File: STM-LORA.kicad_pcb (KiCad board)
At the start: 2 copper layers, 56.5 x 50.8 mm, 22 parts, among them J1 Batt, J11 CONN_02X09, J13 CONN_01X02, J2 Solar, J3 CONN_01X17, J4 CONN_01X03, J6 CONN_01X01, J9 CONN_01X05, U1 stm32f103c8t6-module-china, U2 RFM95HW

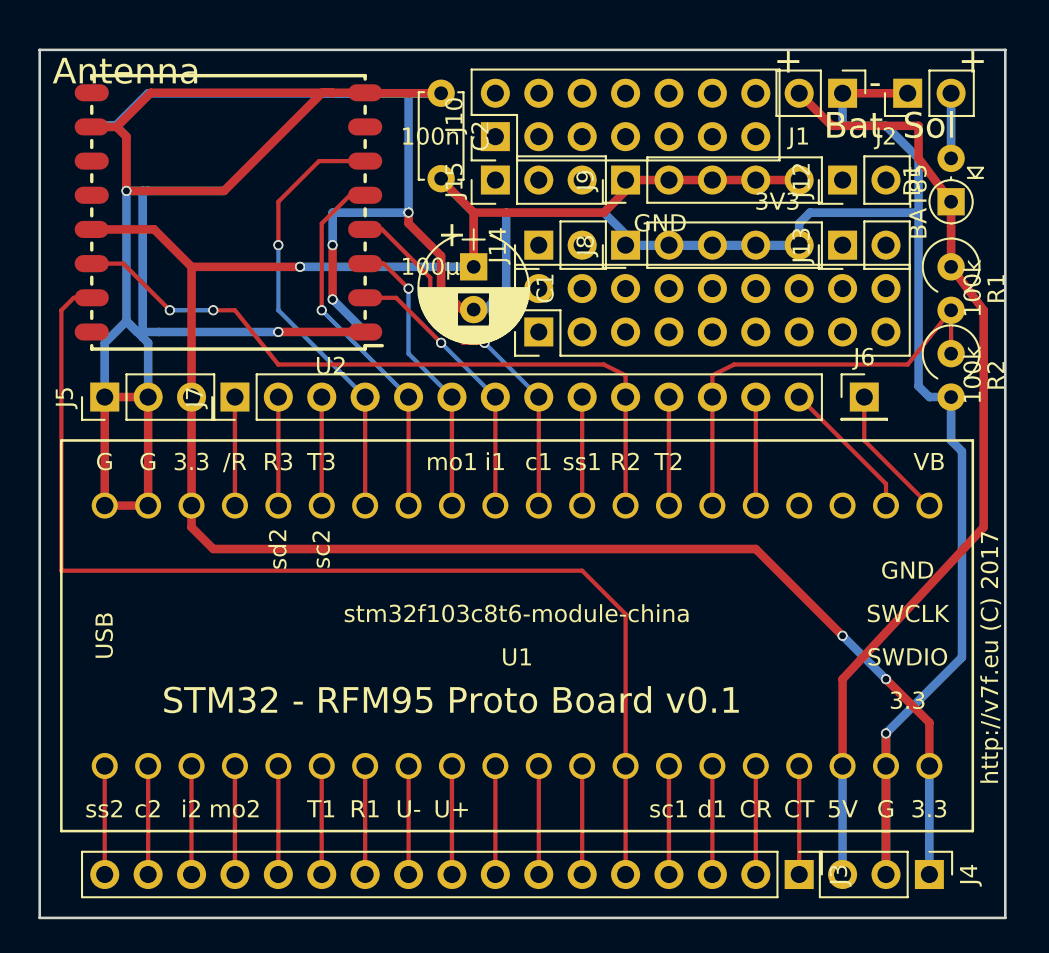
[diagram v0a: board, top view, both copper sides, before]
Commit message: increase power track/via size
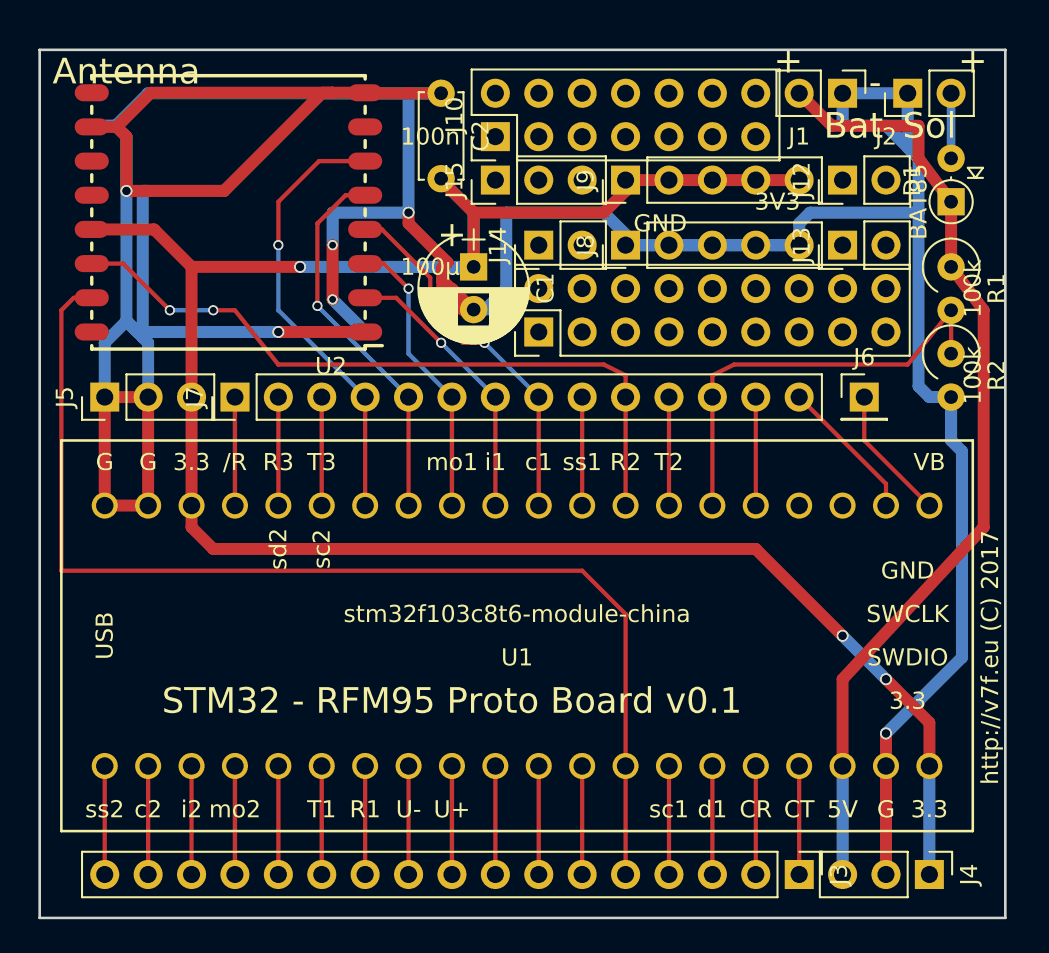
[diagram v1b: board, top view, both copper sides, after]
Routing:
- net GND: track 280.9 -> 290.1 mm
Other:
- net class Power: trace_width 0.5 -> 0.7; via_dia 0.6 -> 0.7; via_drill 0.4 -> 0.5

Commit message: gnd backplane
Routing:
- net GND: track 290.1 -> 21.8 mm, vias 6 -> 4
- added copper zone on B.Cu, net GND

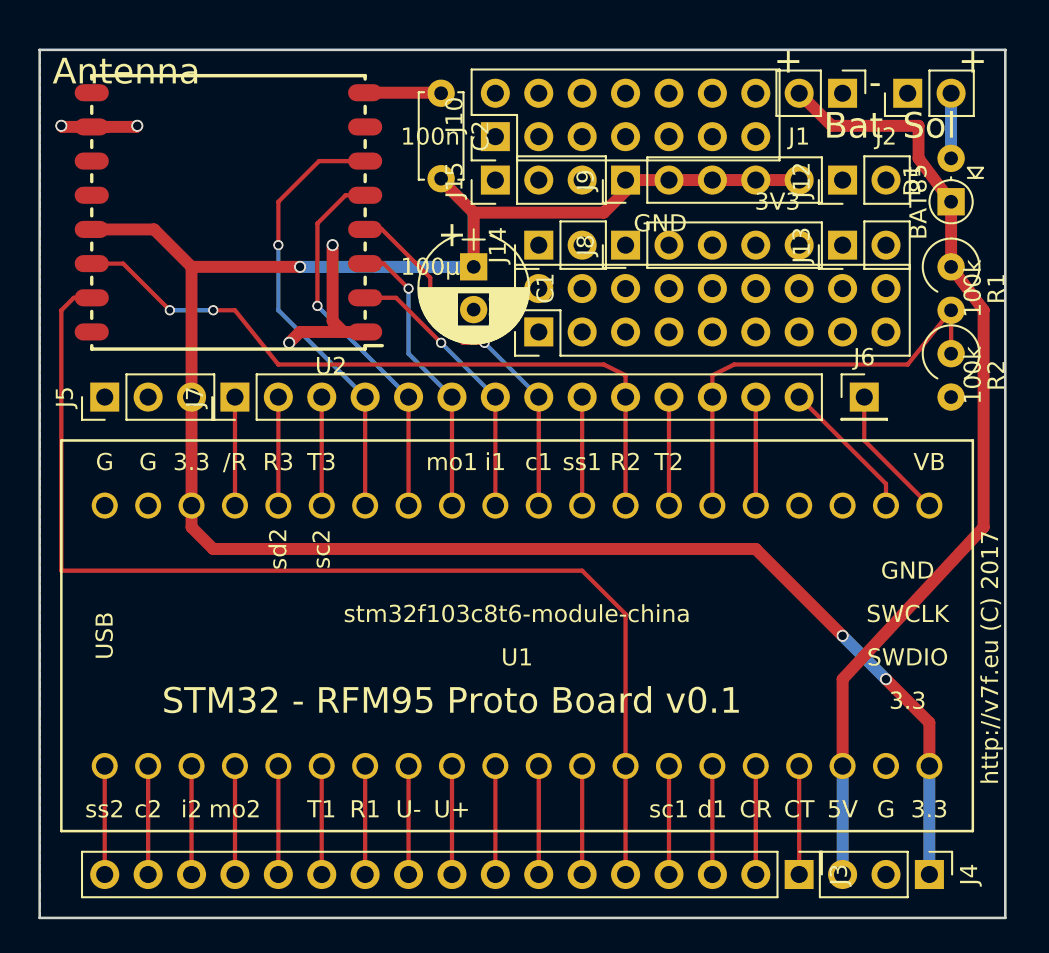
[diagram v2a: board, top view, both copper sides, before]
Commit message: Improve GND backplane
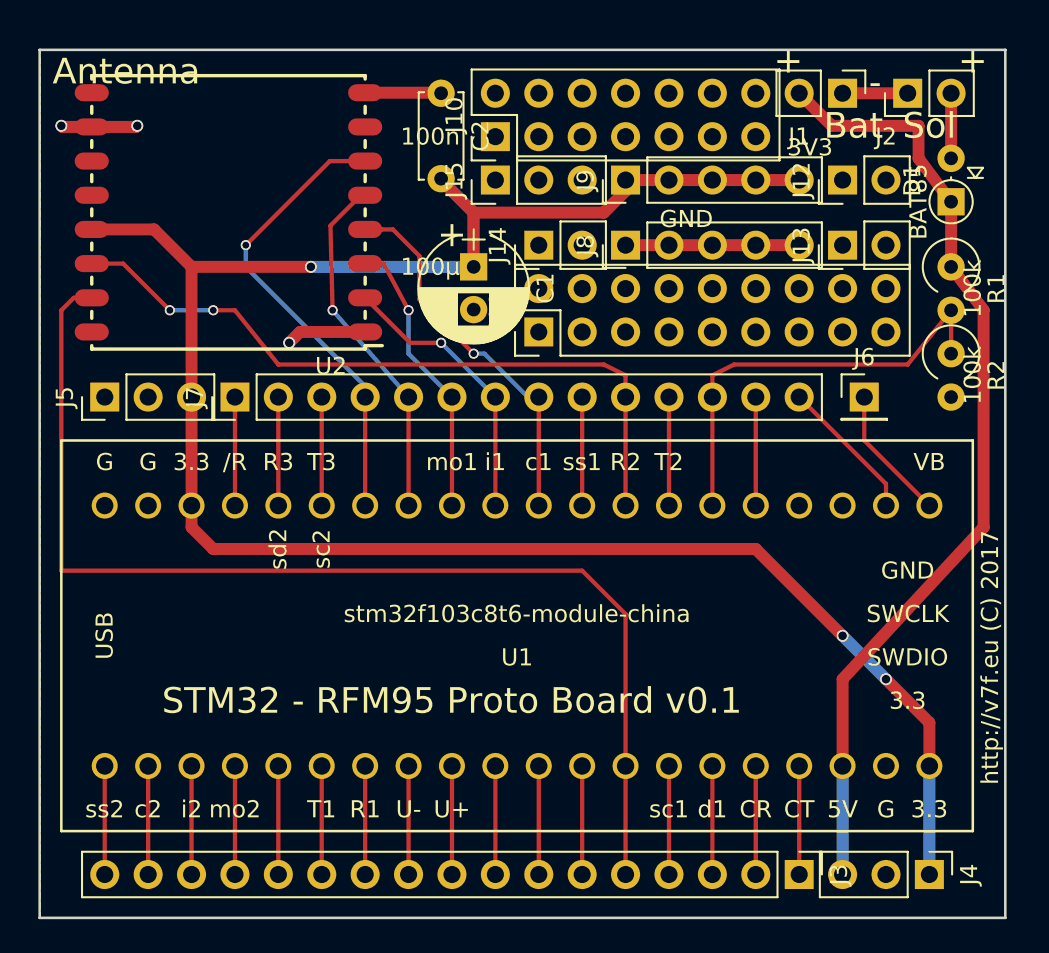
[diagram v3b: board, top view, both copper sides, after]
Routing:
- net /3V3: track 127.4 -> 137.6 mm
- net GND: track 21.8 -> 29.2 mm, vias 4 -> 3
- net /P33: track 22.2 -> 20.8 mm
- net /P30: track 21.7 -> 23.0 mm
- net /P34: track 26.0 -> 27.2 mm
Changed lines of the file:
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@@
-(kicad_pcb (version 4) (host pcbnew 4.0.6-e0-6349~53~ubuntu16.04.1)
+(kicad_pcb (version 4) (host pcbnew 4.0.6)
   (general
     (links 75)
     (no_connects 0)
-    (area 83.744999 55.804999 140.410001 106.755001)
+    (area 83.744999 55.315 141.390371 109.173333)
     (thickness 1.6)
     (drawings 20)
-    (tracks 146)
+    (tracks 147)
     (zones 0)
     (modules 22)
@@
     (aux_axis_origin 0 0)
     (grid_origin 83.82 55.88)
-    (visible_elements 7FFFFFFF)
+    (visible_elements 7FFFBFFF)
     (pcbplotparams
       (layerselection 0x010e0_80000001)
@@
     (effects (font (size 1 1) (thickness 0.2)))
   )
-  (gr_text 3V3 (at 127 64.77) (layer F.SilkS)
+  (gr_text 3V3 (at 128.905 61.595) (layer F.SilkS)
     (effects (font (size 1 1) (thickness 0.2)))
   )
-  (gr_text GND (at 120.142 66.04) (layer F.SilkS)
+  (gr_text GND (at 121.666 65.786) (layer F.SilkS)
     (effects (font (size 1 1) (thickness 0.2)))
   )
@@
     (effects (font (size 1 1) (thickness 0.2)))
   )
+  (segment (start 130.81 58.42) (end 134.62 58.42) (width 0.7) (layer F.Cu) (net 8))
+  (segment (start 118.11 67.31) (end 128.27 67.31) (width 0.7) (layer F.Cu) (net 8))
   (segment (start 86.87 60.39) (end 85.155 60.39) (width 0.7) (layer F.Cu) (net 8))
   (via (at 85.09 60.325) (size 0.7) (drill 0.5) (layers F.Cu B.Cu) (net 8))
@@
   (segment (start 102.87 58.39) (end 107.285 58.39) (width 0.7) (layer F.Cu) (net 8))
   (segment (start 107.285 58.39) (end 107.315 58.42) (width 0.7) (layer F.Cu) (net 8))
-  (segment (start 102.87 72.39) (end 101.6 72.39) (width 0.7) (layer F.Cu) (net 8))
-  (via (at 100.965 67.31) (size 0.7) (drill 0.5) (layers F.Cu B.Cu) (net 8))
-  (segment (start 100.965 71.755) (end 100.965 67.31) (width 0.7) (layer F.Cu) (net 8))
-  (segment (start 101.6 72.39) (end 100.965 71.755) (width 0.7) (layer F.Cu) (net 8))
   (via (at 98.425 73.025) (size 0.7) (drill 0.5) (layers F.Cu B.Cu) (net 8))
   (segment (start 102.87 72.39) (end 99.06 72.39) (width 0.7) (layer F.Cu) (net 8))
@@
   (segment (start 90.17 97.79) (end 90.17 104.14) (width 0.25) (layer F.Cu) (net 25))
   (segment (start 87.63 104.14) (end 87.63 97.79) (width 0.25) (layer F.Cu) (net 26))
+  (segment (start 118.11 63.5) (end 128.27 63.5) (width 0.7) (layer B.Cu) (net 27))
   (segment (start 135.89 97.79) (end 135.89 104.14) (width 0.7) (layer B.Cu) (net 27))
   (segment (start 109.22 68.58) (end 109.22 65.405) (width 0.7) (layer B.Cu) (net 27))
@@
   (via (at 133.35 92.71) (size 0.7) (drill 0.5) (layers F.Cu B.Cu) (net 27))
   (segment (start 135.89 95.25) (end 133.35 92.71) (width 0.7) (layer F.Cu) (net 27))
-  (segment (start 109.22 68.58) (end 99.06 68.58) (width 0.7) (layer B.Cu) (net 27))
-  (segment (start 99.06 68.58) (end 92.71 68.58) (width 0.7) (layer F.Cu) (net 27))
-  (via (at 99.06 68.58) (size 0.7) (drill 0.5) (layers F.Cu B.Cu) (net 27))
+  (segment (start 109.22 68.58) (end 99.695 68.58) (width 0.7) (layer B.Cu) (net 27))
+  (segment (start 99.695 68.58) (end 92.71 68.58) (width 0.7) (layer F.Cu) (net 27))
+  (via (at 99.695 68.58) (size 0.7) (drill 0.5) (layers F.Cu B.Cu) (net 27))
   (segment (start 86.87 66.39) (end 90.52 66.39) (width 0.7) (layer F.Cu) (net 27))
   (segment (start 92.71 68.58) (end 92.71 76.2) (width 0.7) (layer F.Cu) (net 27))
@@
   (segment (start 97.79 82.55) (end 97.79 76.2) (width 0.25) (layer F.Cu) (net 30))
   (segment (start 100.33 82.55) (end 100.33 76.2) (width 0.25) (layer F.Cu) (net 31))
+  (segment (start 102.87 62.39) (end 100.805 62.39) (width 0.25) (layer F.Cu) (net 32))
+  (segment (start 95.885 68.58) (end 95.885 67.31) (width 0.25) (layer B.Cu) (net 32))
+  (segment (start 95.885 68.58) (end 102.87 75.565) (width 0.25) (layer B.Cu) (net 32))
+  (via (at 95.885 67.31) (size 0.6) (drill 0.4) (layers F.Cu B.Cu) (net 32))
+  (segment (start 100.805 62.39) (end 95.885 67.31) (width 0.25) (layer F.Cu) (net 32))
+  (segment (start 102.87 76.2) (end 102.87 75.565) (width 0.25) (layer B.Cu) (net 32))
   (via (at 102.87 76.2) (size 0.6) (drill 0.4) (layers F.Cu B.Cu) (net 32))
-  (segment (start 102.87 76.2) (end 97.79 71.12) (width 0.25) (layer B.Cu) (net 32))
-  (segment (start 100.17 62.39) (end 102.87 62.39) (width 0.25) (layer F.Cu) (net 32))
-  (segment (start 97.79 64.77) (end 100.17 62.39) (width 0.25) (layer F.Cu) (net 32))
-  (segment (start 97.79 67.31) (end 97.79 64.77) (width 0.25) (layer F.Cu) (net 32))
-  (via (at 97.79 67.31) (size 0.6) (drill 0.4) (layers F.Cu B.Cu) (net 32))
-  (segment (start 97.79 71.12) (end 97.79 67.31) (width 0.25) (layer B.Cu) (net 32))
   (segment (start 102.87 82.55) (end 102.87 76.2) (width 0.25) (layer F.Cu) (net 32))
   (via (at 105.41 76.2) (size 0.6) (drill 0.4) (layers F.Cu B.Cu) (net 33))
-  (segment (start 105.41 76.2) (end 100.076 70.866) (width 0.25) (layer B.Cu) (net 33))
-  (segment (start 100.076 66.04) (end 101.726 64.39) (width 0.25) (layer F.Cu) (net 33))
-  (segment (start 100.076 70.866) (end 100.076 66.04) (width 0.25) (layer F.Cu) (net 33))
-  (via (at 100.076 70.866) (size 0.6) (drill 0.4) (layers F.Cu B.Cu) (net 33))
-  (segment (start 101.726 64.39) (end 102.87 64.39) (width 0.25) (layer F.Cu) (net 33))
+  (segment (start 105.41 76.2) (end 100.965 71.12) (width 0.25) (layer B.Cu) (net 33))
+  (segment (start 100.838 66.167) (end 102.488 64.517) (width 0.25) (layer F.Cu) (net 33))
+  (segment (start 100.965 71.12) (end 100.838 66.167) (width 0.25) (layer F.Cu) (net 33))
+  (via (at 100.965 71.12) (size 0.6) (drill 0.4) (layers F.Cu B.Cu) (net 33))
+  (segment (start 102.488 64.517) (end 102.87 64.39) (width 0.25) (layer F.Cu) (net 33))
   (segment (start 105.41 82.55) (end 105.41 76.2) (width 0.25) (layer F.Cu) (net 33))
   (via (at 107.95 76.2) (size 0.6) (drill 0.4) (layers F.Cu B.Cu) (net 34))
   (segment (start 107.95 76.2) (end 105.41 73.66) (width 0.25) (layer B.Cu) (net 34))
   (segment (start 103.95 68.39) (end 102.87 68.39) (width 0.25) (layer F.Cu) (net 34))
-  (segment (start 105.41 69.85) (end 103.95 68.39) (width 0.25) (layer F.Cu) (net 34))
-  (via (at 105.41 69.85) (size 0.6) (drill 0.4) (layers F.Cu B.Cu) (net 34))
-  (segment (start 105.41 73.66) (end 105.41 69.85) (width 0.25) (layer B.Cu) (net 34))
+  (segment (start 105.41 71.12) (end 103.95 68.39) (width 0.25) (layer F.Cu) (net 34))
+  (via (at 105.41 71.12) (size 0.6) (drill 0.4) (layers F.Cu B.Cu) (net 34))
+  (segment (start 105.41 73.66) (end 105.41 71.12) (width 0.25) (layer B.Cu) (net 34))
   (segment (start 107.95 82.55) (end 107.95 76.2) (width 0.25) (layer F.Cu) (net 34))
+  (segment (start 107.315 73.025) (end 105.505 73.025) (width 0.25) (layer F.Cu) (net 35))
+  (segment (start 105.505 73.025) (end 102.87 70.39) (width 0.25) (layer F.Cu) (net 35))
   (segment (start 110.49 76.2) (end 107.315 73.025) (width 0.25) (layer B.Cu) (net 35))
-  (segment (start 104.68 70.39) (end 102.87 70.39) (width 0.25) (layer F.Cu) (net 35))
-  (segment (start 107.315 73.025) (end 104.68 70.39) (width 0.25) (layer F.Cu) (net 35))
   (via (at 107.315 73.025) (size 0.6) (drill 0.4) (layers F.Cu B.Cu) (net 35))
   (via (at 110.49 76.2) (size 0.6) (drill 0.4) (layers F.Cu B.Cu) (net 35))
   (segment (start 110.49 82.55) (end 110.49 76.2) (width 0.25) (layer F.Cu) (net 35))
+  (segment (start 113.03 76.2) (end 112.395 76.2) (width 0.25) (layer B.Cu) (net 36))
+  (segment (start 112.395 76.2) (end 109.855 73.66) (width 0.25) (layer B.Cu) (net 36))
+  (segment (start 104.49 66.39) (end 102.87 66.39) (width 0.25) (layer F.Cu) (net 36))
+  (segment (start 106.045 67.945) (end 104.49 66.39) (width 0.25) (layer F.Cu) (net 36))
+  (segment (start 106.045 70.485) (end 106.045 67.945) (width 0.25) (layer F.Cu) (net 36))
+  (segment (start 109.22 73.66) (end 106.045 70.485) (width 0.25) (layer F.Cu) (net 36))
+  (via (at 109.22 73.66) (size 0.6) (drill 0.4) (layers F.Cu B.Cu) (net 36))
+  (segment (start 109.855 73.66) (end 109.22 73.66) (width 0.25) (layer B.Cu) (net 36))
   (via (at 113.03 76.2) (size 0.6) (drill 0.4) (layers F.Cu B.Cu) (net 36))
-  (segment (start 113.03 76.2) (end 109.855 73.025) (width 0.25) (layer B.Cu) (net 36))
-  (segment (start 106.68 69.215) (end 103.855 66.39) (width 0.25) (layer F.Cu) (net 36))
-  (segment (start 106.68 71.12) (end 106.68 69.215) (width 0.25) (layer F.Cu) (net 36))
-  (segment (start 108.585 73.025) (end 106.68 71.12) (width 0.25) (layer F.Cu) (net 36))
-  (segment (start 109.855 73.025) (end 108.585 73.025) (width 0.25) (layer F.Cu) (net 36))
-  (via (at 109.855 73.025) (size 0.6) (drill 0.4) (layers F.Cu B.Cu) (net 36))
   (segment (start 103.855 66.39) (end 102.87 66.39) (width 0.25) (layer F.Cu) (net 36))
   (segment (start 113.03 82.55) (end 113.03 76.2) (width 0.25) (layer F.Cu) (net 36))
@@
   (segment (start 133.35 82.55) (end 133.35 81.28) (width 0.25) (layer F.Cu) (net 42))
   (segment (start 133.35 81.28) (end 128.27 76.2) (width 0.25) (layer F.Cu) (net 42))
-  (segment (start 137.16 58.42) (end 137.16 62.23) (width 0.7) (layer B.Cu) (net 43))
+  (segment (start 137.16 58.42) (end 137.16 62.23) (width 0.7) (layer F.Cu) (net 43))
   (zone (net 8) (net_name GND) (layer B.Cu) (hatch edge 0.508)
     (connect_pads (clearance 0.508))

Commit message: improve GND plane and double 3V3 track
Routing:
- net /3V3: track 137.6 -> 180.8 mm, vias 3 -> 7
- net /P26: track 25.8 -> 27.9 mm
- net /P31: track 16.4 -> 15.8 mm
